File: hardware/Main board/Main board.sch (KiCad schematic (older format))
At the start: 98 parts, among them J1 Wind Direction, J10 Free Pins, J11 Nokia 5110 LCD, J2 Wind Speed, J3 USB_B_Micro, J4 Micro_SD_Card, J5 Sensor board connector, J6 Barrel_Jack, J7 ISP programmer, J8 SPI1, J9 SPI2, Q1 IRLML2060, SW1 SW_Push, SW2 SW_SPST, SW3 SW_Push, SW4 SW_Push, SW5 Page Switch btn, SW6 LCD rst btn, U1 FT232RL, U2 MCP6042, U3 SCWN03A-03, U4 ATmega1284P-AU, U5 DS3231MZ, U6 ENC28J60, U7 USB6B1, U8 DRV5053, Y1 16MHZ

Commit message: Updated main board
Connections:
- net labels removed: +3V3
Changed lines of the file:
@@
 	7950 4050 8250 4050
-$Comp
-L power:+3V3 #PWR035
-U 1 1 5D3242DE
-P 7950 3850
-F 0 "#PWR035" H 7950 3700 50  0001 C CNN
-F 1 "+3V3" H 7965 4023 50  0000 C CNN
-F 2 "" H 7950 3850 50  0001 C CNN
-F 3 "" H 7950 3850 50  0001 C CNN
-	1    7950 3850
-	1    0    0    -1
-$EndComp
-$Comp
-L power:+3V3 #PWR036
-U 1 1 5D324CF7
-P 7950 4350
-F 0 "#PWR036" H 7950 4200 50  0001 C CNN
-F 1 "+3V3" H 7965 4523 50  0000 C CNN
-F 2 "" H 7950 4350 50  0001 C CNN
-F 3 "" H 7950 4350 50  0001 C CNN
-	1    7950 4350
-	-1   0    0    1
-$EndComp
 $Comp
 L Device:C_Small C12
@@
 Wire Wire Line
 	1500 6400 1050 6400
+$Comp
+L power:VCC #PWR?
+U 1 1 5D902AAA
+P 7950 3850
+F 0 "#PWR?" H 7950 3700 50  0001 C CNN
+F 1 "VCC" V 7967 3978 50  0000 L CNN
+F 2 "" H 7950 3850 50  0001 C CNN
+F 3 "" H 7950 3850 50  0001 C CNN
+	1    7950 3850
+	1    0    0    -1
+$EndComp
+$Comp
+L power:VCC #PWR?
+U 1 1 5D902F05
+P 7950 4350
+F 0 "#PWR?" H 7950 4200 50  0001 C CNN
+F 1 "VCC" V 7967 4478 50  0000 L CNN
+F 2 "" H 7950 4350 50  0001 C CNN
+F 3 "" H 7950 4350 50  0001 C CNN
+	1    7950 4350
+	-1   0    0    1
+$EndComp
 $EndSCHEMATC

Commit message: Finished the board design
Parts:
- removed C18: 4.7uF, Capacitor_SMD:C_0805_2012Metric_Pad1.15x1.40mm_HandSolder, symbol Device:C_Small
- added C18: 4.7uF, Capacitor_SMD:C_0805_2012Metric_Pad1.15x1.40mm_HandSolder, symbol Device:CP_Small
- added D11: PWR_LED, Diode_SMD:D_0805_2012Metric, symbol Device:LED
- added R34: 55, Resistor_SMD:R_0805_2012Metric, symbol Device:R_Small
- added TP1: WindDir, Meteo_Footprints:Test_Pad, symbol Connector:TestPoint
- added TP2: WindSpeed, Meteo_Footprints:Test_Pad, symbol Connector:TestPoint
- BT1: footprint Battery:BatteryHolder_Keystone_103_1x20mm -> Battery:BatteryHolder_Keystone_106_1x20mm
- J10: footprint TerminalBlock_Phoenix:TerminalBlock_Phoenix_MKDS-1,5-6_1x06_P5.00mm_Horizontal -> TerminalBlock_Phoenix:TerminalBlock_Phoenix_MKDS-1,5-8_1x08_P5.00mm_Horizontal; symbol Connector:Screw_Terminal_01x05 -> Connector:Screw_Terminal_01x08
- J11: footprint Connector_PinHeader_2.54mm:PinHeader_1x08_P2.54mm_Vertical -> Meteo_Footprints:Nokia_5110_LCD
- J3: footprint Connector_USB:USB_Micro-B_Molex-105017-0001 -> Meteo_Footprints:KYCON_KMMVX-SMT-BS-BTR; symbol Connector:USB_B_Micro -> Meteo_Station:USB_B_Micro
- U8: footprint Package_TO_SOT_THT:TO-92 -> Connector_PinSocket_2.54mm:PinSocket_1x03_P2.54mm_Vertical
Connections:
- wire segments 196 -> 198
- no-connect marks 24 -> 23

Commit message: Added 0 new easter eggs
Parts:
- added C25: 4.7uF, Capacitor_SMD:CP_Elec_4x5.4, symbol Device:CP_Small
- C18: footprint Capacitor_SMD:C_0805_2012Metric_Pad1.15x1.40mm_HandSolder -> Capacitor_SMD:CP_Elec_4x5.3
- J6: symbol Connector:Barrel_Jack -> Connector:Barrel_Jack_MountingPin
- SW1, SW3, SW4, SW5, SW6: footprint Button_Switch_SMD:SW_SPST_B3S-1100 -> Button_Switch_SMD:SW_Push_1P1T_NO_6x6mm_H9.5mm
- Y1: footprint Crystal:Crystal_SMD_EuroQuartz_MT-4Pin_3.2x2.5mm -> Meteo_Footprints:Crystal_SMD; symbol Device:Crystal_Small -> Device:Crystal_GND24_Small
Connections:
- net GND: now also J4.9 (SHIELD), J6.MP (MountPin), Y1.2, Y1.4, C25.2
- net VCC: now also C25.1
- net at C8.2, U4.7 (XTAL2): now also Y1.3; no longer Y1.2
- no-connect marks 23 -> 22
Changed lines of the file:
@@
 F 0 "SW1" H 6150 2285 50  0000 C CNN
 F 1 "SW_Push" H 6150 2194 50  0000 C CNN
-F 2 "Button_Switch_SMD:SW_SPST_B3S-1100" H 6150 2200 50  0001 C CNN
+F 2 "Button_Switch_SMD:SW_Push_1P1T_NO_6x6mm_H9.5mm" H 6150 2200 50  0001 C CNN
 F 3 "~" H 6150 2200 50  0001 C CNN
 	1    6150 2000
@@
 $EndComp
 $Comp
-L Device:Crystal_Small Y1
+L Device:Crystal_GND24_Small Y1
 U 1 1 5D39118F
-P 5900 2550
-F 0 "Y1" V 5869 2638 50  0000 L CNN
-F 1 "16MHZ" V 5946 2638 31  0000 L CNN
-F 2 "Crystal:Crystal_SMD_EuroQuartz_MT-4Pin_3.2x2.5mm" H 5900 2550 50  0001 C CNN
-F 3 "~" H 5900 2550 50  0001 C CNN
-	1    5900 2550
-	0    1    1    0
-$EndComp
-Wire Wire Line
-	6350 2450 5900 2450
-Wire Wire Line
-	6350 2650 5900 2650
+P 6000 2550
+F 0 "Y1" V 5969 2638 50  0000 L CNN
+F 1 "16MHZ" V 6050 2300 31  0000 L CNN
+F 2 "Meteo_Footprints:Crystal_SMD" H 6000 2550 50  0001 C CNN
+F 3 "~" H 6000 2550 50  0001 C CNN
+	1    6000 2550
+	0    1    1    0
+$EndComp
+Wire Wire Line
+	6350 2450 6000 2450
+Wire Wire Line
+	6350 2650 6000 2650
 $Comp
 L Device:C_Small C7
@@
 	0    -1   -1   0
 $EndComp
-Wire Wire Line
-	5800 2450 5900 2450
-Connection ~ 5900 2450
-Wire Wire Line
-	5800 2650 5900 2650
-Connection ~ 5900 2650
 Wire Wire Line
 	5600 2450 5600 2650
@@
 NoConn ~ 9900 900
 $Comp
-L Connector:Barrel_Jack J6
+L Connector:Barrel_Jack_MountingPin J6
 U 1 1 5D473214
 P 4000 1000
@@
 NoConn ~ 9400 4350
 NoConn ~ 8400 4750
-NoConn ~ 11150 3300
 $Comp
 L Device:R_Small R10
@@
 F 0 "SW3" H 8150 6385 50  0000 C CNN
 F 1 "SW_Push" H 8150 6294 50  0000 C CNN
-F 2 "Button_Switch_SMD:SW_SPST_B3S-1100" H 8150 6300 50  0001 C CNN
+F 2 "Button_Switch_SMD:SW_Push_1P1T_NO_6x6mm_H9.5mm" H 8150 6300 50  0001 C CNN
 F 3 "~" H 8150 6300 50  0001 C CNN
 	1    8150 6100
@@
 F 0 "SW4" H 9100 6385 50  0000 C CNN
 F 1 "SW_Push" H 9100 6294 50  0000 C CNN
-F 2 "Button_Switch_SMD:SW_SPST_B3S-1100" H 9100 6300 50  0001 C CNN
+F 2 "Button_Switch_SMD:SW_Push_1P1T_NO_6x6mm_H9.5mm" H 9100 6300 50  0001 C CNN
 F 3 "~" H 9100 6300 50  0001 C CNN
 	1    9100 6100
@@
 F 0 "SW5" H 2850 6850 50  0000 C CNN
 F 1 "Page Switch btn" H 2850 6750 50  0000 C CNN
-F 2 "Button_Switch_SMD:SW_SPST_B3S-1100" H 2750 6750 50  0001 C CNN
+F 2 "Button_Switch_SMD:SW_Push_1P1T_NO_6x6mm_H9.5mm" H 2750 6750 50  0001 C CNN
 F 3 "~" H 2750 6750 50  0001 C CNN
 	1    2750 6550
@@
 F 0 "SW6" H 2000 7535 50  0000 C CNN
 F 1 "LCD rst btn" H 2000 7444 50  0000 C CNN
-F 2 "Button_Switch_SMD:SW_SPST_B3S-1100" H 2000 7450 50  0001 C CNN
+F 2 "Button_Switch_SMD:SW_Push_1P1T_NO_6x6mm_H9.5mm" H 2000 7450 50  0001 C CNN
 F 3 "~" H 2000 7450 50  0001 C CNN
 	1    2000 7250
@@
 F 0 "C18" H 3562 3304 50  0000 R CNN
 F 1 "4.7uF" H 3562 3395 50  0000 R CNN
-F 2 "Capacitor_SMD:C_0805_2012Metric_Pad1.15x1.40mm_HandSolder" H 3650 3350 50  0001 C CNN
+F 2 "Capacitor_SMD:CP_Elec_4x5.3" H 3650 3350 50  0001 C CNN
 F 3 "~" H 3650 3350 50  0001 C CNN
 	1    3650 3350
@@
 Wire Wire Line
 	6250 800  6250 750
+$Comp
+L power:GND #PWR0118
+U 1 1 5D3AC36E
+P 4000 1300
+F 0 "#PWR0118" H 4000 1050 50  0001 C CNN
+F 1 "GND" V 4005 1172 50  0000 R CNN
+F 2 "" H 4000 1300 50  0001 C CNN
+F 3 "" H 4000 1300 50  0001 C CNN
+	1    4000 1300
+	1    0    0    -1
+$EndComp
+$Comp
+L power:GND #PWR0119
+U 1 1 5D3AC7E0
+P 11150 3300
+F 0 "#PWR0119" H 11150 3050 50  0001 C CNN
+F 1 "GND" H 11155 3127 50  0000 C CNN
+F 2 "" H 11150 3300 50  0001 C CNN
+F 3 "" H 11150 3300 50  0001 C CNN
+	1    11150 3300
+	1    0    0    -1
+$EndComp
+Wire Wire Line
+	9100 2700 8850 2700
+Wire Wire Line
+	8850 2900 9100 2900
+$Comp
+L Device:CP_Small C25
+U 1 1 5D3D1832
+P 8850 2800
+F 0 "C25" H 8762 2754 50  0000 R CNN
+F 1 "4.7uF" H 8762 2845 50  0000 R CNN
+F 2 "Capacitor_SMD:CP_Elec_4x5.4" H 8850 2800 50  0001 C CNN
+F 3 "~" H 8850 2800 50  0001 C CNN
+	1    8850 2800
+	1    0    0    -1
+$EndComp
+$Comp
+L power:GND #PWR0120
+U 1 1 5D4F2EEF
+P 6150 2550
+F 0 "#PWR0120" H 6150 2300 50  0001 C CNN
+F 1 "GND" H 6155 2377 50  0000 C CNN
+F 2 "" H 6150 2550 50  0001 C CNN
+F 3 "" H 6150 2550 50  0001 C CNN
+	1    6150 2550
+	0    -1   -1   0
+$EndComp
+Connection ~ 6000 2650
+Wire Wire Line
+	5800 2650 6000 2650
+Wire Wire Line
+	5800 2450 6000 2450
+Connection ~ 6000 2450
+Wire Wire Line
+	6150 2550 6100 2550
+$Comp
+L power:GND #PWR0121
+U 1 1 5D52432F
+P 5850 2550
+F 0 "#PWR0121" H 5850 2300 50  0001 C CNN
+F 1 "GND" V 5800 2550 31  0000 C CNN
+F 2 "" H 5850 2550 50  0001 C CNN
+F 3 "" H 5850 2550 50  0001 C CNN
+	1    5850 2550
+	0    1    1    0
+$EndComp
+Wire Wire Line
+	5850 2550 5900 2550
 $EndSCHEMATC

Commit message: Added 0 new easter eggs
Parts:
- removed C24: 100nF, Capacitor_SMD:C_0805_2012Metric_Pad1.15x1.40mm_HandSolder, symbol Device:C_Small
- removed R32: 100k, Resistor_SMD:R_0805_2012Metric, symbol Device:R_Small
- removed SW6: LCD rst btn, Button_Switch_SMD:SW_Push_1P1T_NO_6x6mm_H9.5mm, symbol Switch:SW_Push
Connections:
- net GND: now also J10.5 (Pin_5); no longer J10.6 (Pin_6)
- net PC2: now also J11.1 (Pin_1); no longer J10.5 (Pin_5)
- net VCC: now also J10.6 (Pin_6)
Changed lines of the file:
@@
 Text GLabel 3800 7100 1    50   Input ~ 0
 PB0
-Text GLabel 5700 7100 1    50   Input ~ 0
+Text GLabel 1050 7000 2    50   Input ~ 0
 PC2
 Text GLabel 1050 6800 2    50   Input ~ 0
@@
 	5400 6100 5400 6200
 Connection ~ 5400 6100
-$Comp
-L Switch:SW_Push SW6
-U 1 1 5D44CBC3
-P 2000 7250
-F 0 "SW6" H 2000 7535 50  0000 C CNN
-F 1 "LCD rst btn" H 2000 7444 50  0000 C CNN
-F 2 "Button_Switch_SMD:SW_Push_1P1T_NO_6x6mm_H9.5mm" H 2000 7450 50  0001 C CNN
-F 3 "~" H 2000 7450 50  0001 C CNN
-	1    2000 7250
-	1    0    0    -1
-$EndComp
-$Comp
-L power:GND #PWR0109
-U 1 1 5D44D1E7
-P 2200 7450
-F 0 "#PWR0109" H 2200 7200 50  0001 C CNN
-F 1 "GND" V 2205 7322 50  0000 R CNN
-F 2 "" H 2200 7450 50  0001 C CNN
-F 3 "" H 2200 7450 50  0001 C CNN
-	1    2200 7450
-	0    -1   -1   0
-$EndComp
-$Comp
-L Device:C_Small C24
-U 1 1 5D44D6FE
-P 2000 7450
-F 0 "C24" V 1900 7450 50  0000 C CNN
-F 1 "100nF" V 1850 7450 31  0000 C CNN
-F 2 "Capacitor_SMD:C_0805_2012Metric_Pad1.15x1.40mm_HandSolder" H 2000 7450 50  0001 C CNN
-F 3 "~" H 2000 7450 50  0001 C CNN
-	1    2000 7450
-	0    -1   -1   0
-$EndComp
-$Comp
-L Device:R_Small R32
-U 1 1 5D44DC92
-P 1550 7150
-F 0 "R32" H 1609 7196 50  0000 L CNN
-F 1 "100k" H 1609 7105 50  0000 L CNN
-F 2 "Resistor_SMD:R_0805_2012Metric" H 1550 7150 50  0001 C CNN
-F 3 "~" H 1550 7150 50  0001 C CNN
-	1    1550 7150
-	1    0    0    -1
-$EndComp
-$Comp
-L power:VCC #PWR0110
-U 1 1 5D44E1D7
-P 1550 7050
-F 0 "#PWR0110" H 1550 6900 50  0001 C CNN
-F 1 "VCC" V 1568 7177 50  0000 L CNN
-F 2 "" H 1550 7050 50  0001 C CNN
-F 3 "" H 1550 7050 50  0001 C CNN
-	1    1550 7050
-	1    0    0    -1
-$EndComp
-Wire Wire Line
-	1050 7000 1050 7450
-Wire Wire Line
-	1050 7450 1550 7450
-Wire Wire Line
-	1550 7250 1550 7450
-Connection ~ 1550 7450
-Wire Wire Line
-	1550 7450 1900 7450
-Wire Wire Line
-	1550 7250 1800 7250
-Connection ~ 1550 7250
-Wire Wire Line
-	2200 7250 2200 7450
-Wire Wire Line
-	2100 7450 2200 7450
-Connection ~ 2200 7450
 Wire Wire Line
 	2100 4200 2600 4200
@@
 L power:GND #PWR0116
 U 1 1 5D5097B1
-P 5600 7100
-F 0 "#PWR0116" H 5600 6850 50  0001 C CNN
-F 1 "GND" V 5605 6972 50  0000 R CNN
-F 2 "" H 5600 7100 50  0001 C CNN
-F 3 "" H 5600 7100 50  0001 C CNN
-	1    5600 7100
+P 5700 7100
+F 0 "#PWR0116" H 5700 6850 50  0001 C CNN
+F 1 "GND" V 5705 6972 50  0000 R CNN
+F 2 "" H 5700 7100 50  0001 C CNN
+F 3 "" H 5700 7100 50  0001 C CNN
+	1    5700 7100
 	-1   0    0    1
 $EndComp
@@
 Wire Wire Line
 	5850 2550 5900 2550
+$Comp
+L power:VCC #PWR?
+U 1 1 5D634977
+P 5600 7100
+F 0 "#PWR?" H 5600 6950 50  0001 C CNN
+F 1 "VCC" V 5618 7227 50  0000 L CNN
+F 2 "" H 5600 7100 50  0001 C CNN
+F 3 "" H 5600 7100 50  0001 C CNN
+	1    5600 7100
+	1    0    0    -1
+$EndComp
 $EndSCHEMATC

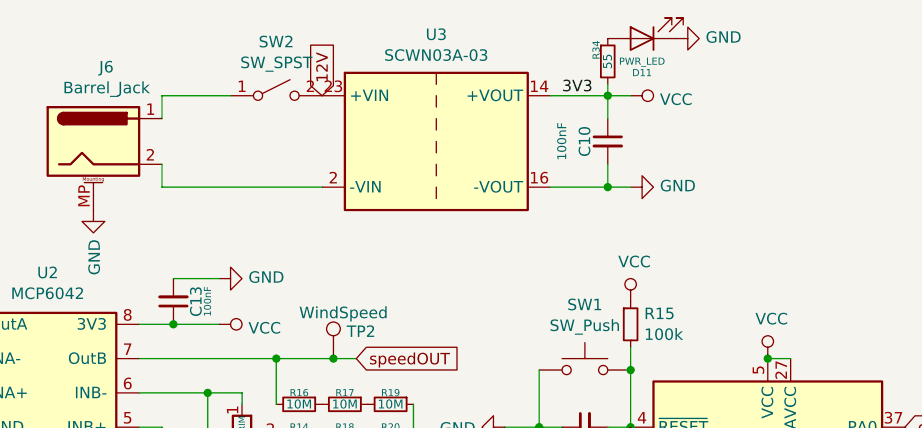
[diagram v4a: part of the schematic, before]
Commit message: Updated the main board to v0.5
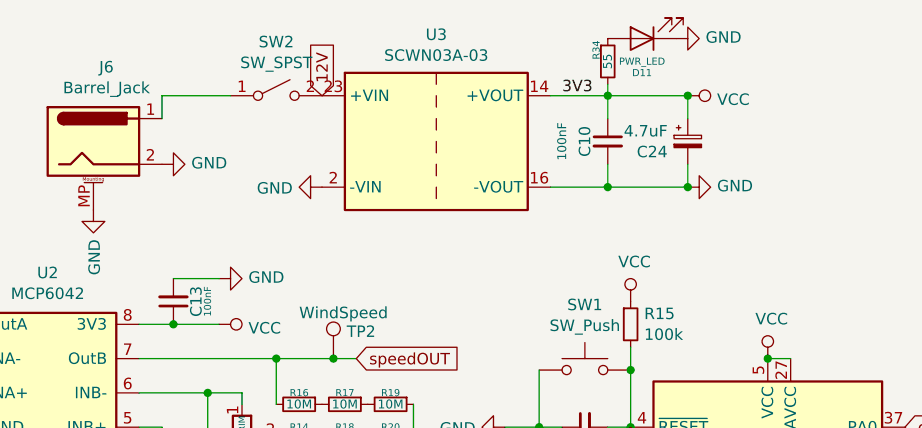
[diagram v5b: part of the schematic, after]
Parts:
- added C24: 4.7uF, Capacitor_SMD:CP_Elec_4x5.4, symbol Device:CP_Small
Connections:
- net GND: now also J6.2, U3.2 (-VIN), C24.2
- net VCC: now also C24.1
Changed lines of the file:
@@
 Connection ~ 6250 800
-Wire Wire Line
-	6250 800  6350 800
 Wire Wire Line
 	6250 1100 6250 1200
 Connection ~ 6250 1200
-Wire Wire Line
-	6250 1200 6350 1200
 Text Label 6050 800  0    50   ~ 0
 3V3
@@
 Wire Wire Line
 	4300 800  4600 800
-Wire Wire Line
-	4300 1100 4300 1200
-Wire Wire Line
-	4300 1200 5000 1200
 $Comp
 L Power_Protection:USB6B1 U7
@@
 L power:GND #PWR031
 U 1 1 5D3744FF
-P 6350 1200
-F 0 "#PWR031" H 6350 950 50  0001 C CNN
-F 1 "GND" V 6355 1072 50  0000 R CNN
-F 2 "" H 6350 1200 50  0001 C CNN
-F 3 "" H 6350 1200 50  0001 C CNN
-	1    6350 1200
+P 6600 1200
+F 0 "#PWR031" H 6600 950 50  0001 C CNN
+F 1 "GND" V 6605 1072 50  0000 R CNN
+F 2 "" H 6600 1200 50  0001 C CNN
+F 3 "" H 6600 1200 50  0001 C CNN
+	1    6600 1200
 	0    -1   -1   0
 $EndComp
@@
 L power:VCC #PWR030
 U 1 1 5D377A4D
-P 6350 800
-F 0 "#PWR030" H 6350 650 50  0001 C CNN
-F 1 "VCC" V 6367 928 50  0000 L CNN
-F 2 "" H 6350 800 50  0001 C CNN
-F 3 "" H 6350 800 50  0001 C CNN
-	1    6350 800
+P 6600 800
+F 0 "#PWR030" H 6600 650 50  0001 C CNN
+F 1 "VCC" V 6617 928 50  0000 L CNN
+F 2 "" H 6600 800 50  0001 C CNN
+F 3 "" H 6600 800 50  0001 C CNN
+	1    6600 800
 	0    1    1    0
 $EndComp
@@
 	5850 2550 5900 2550
 $Comp
-L power:VCC #PWR?
+L power:VCC #PWR0109
 U 1 1 5D634977
 P 5600 7100
-F 0 "#PWR?" H 5600 6950 50  0001 C CNN
+F 0 "#PWR0109" H 5600 6950 50  0001 C CNN
 F 1 "VCC" V 5618 7227 50  0000 L CNN
 F 2 "" H 5600 7100 50  0001 C CNN
@@
 	1    0    0    -1
 $EndComp
+$Comp
+L power:GND #PWR0110
+U 1 1 5D3ED775
+P 4300 1100
+F 0 "#PWR0110" H 4300 850 50  0001 C CNN
+F 1 "GND" V 4305 972 50  0000 R CNN
+F 2 "" H 4300 1100 50  0001 C CNN
+F 3 "" H 4300 1100 50  0001 C CNN
+	1    4300 1100
+	0    -1   -1   0
+$EndComp
+$Comp
+L power:GND #PWR0122
+U 1 1 5D3EDB11
+P 5000 1200
+F 0 "#PWR0122" H 5000 950 50  0001 C CNN
+F 1 "GND" V 5005 1072 50  0000 R CNN
+F 2 "" H 5000 1200 50  0001 C CNN
+F 3 "" H 5000 1200 50  0001 C CNN
+	1    5000 1200
+	0    1    1    0
+$EndComp
+$Comp
+L Device:CP_Small C24
+U 1 1 5D3EE908
+P 6600 1000
+F 0 "C24" H 6512 954 50  0000 R CNN
+F 1 "4.7uF" H 6512 1045 50  0000 R CNN
+F 2 "Capacitor_SMD:CP_Elec_4x5.4" H 6600 1000 50  0001 C CNN
+F 3 "~" H 6600 1000 50  0001 C CNN
+	1    6600 1000
+	1    0    0    -1
+$EndComp
+Wire Wire Line
+	6600 800  6600 900
+Wire Wire Line
+	6250 800  6600 800
+Connection ~ 6600 800
+Wire Wire Line
+	6600 1200 6600 1100
+Wire Wire Line
+	6250 1200 6600 1200
+Connection ~ 6600 1200
 $EndSCHEMATC
